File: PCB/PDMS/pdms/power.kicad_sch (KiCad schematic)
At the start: 32 parts, among them IC10 LDO40LPU50RY, IC11 MP2332HGTL-P, IC14 LDO40LPU50RY, IC3 LDO40LPU33RY, Q1 AO3401A, Q11 AO3401A

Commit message: Finished 2024 version + gerbers
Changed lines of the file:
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@@
   (junction (at 94.615 42.545) (diameter 0) (color 0 0 0 0)
+  )
+  (junction (at 154.813 175.768) (diameter 0) (color 0 0 0 0)
   )
   (junction (at 149.225 45.72) (diameter 0) (color 0 0 0 0)
@@
     (stroke (width 0) (type default) (color 0 0 0 0))
   )
+  (wire (pts (xy 154.813 175.768) (xy 152.527 175.768))
+    (stroke (width 0) (type default) (color 0 0 0 0))
+  )
   (wire (pts (xy 215.265 49.53) (xy 215.265 45.72))
     (stroke (width 0) (type default) (color 0 0 0 0))
@@
     (stroke (width 0) (type default) (color 0 0 0 0))
   )
-  (wire (pts (xy 153.543 175.768) (xy 152.527 175.768))
+  (wire (pts (xy 157.353 175.768) (xy 154.813 175.768))
     (stroke (width 0) (type default) (color 0 0 0 0))
   )
@@
     (pin "1")
   )
-  (symbol (lib_id "power:+12VA") (at 153.543 175.768 270) (unit 1)
-    (in_bom yes) (on_board yes) (fields_autoplaced)
-    (property "Reference" "#PWR0136" (id 0) (at 149.733 175.768 0)
-      (effects (font (size 1.27 1.27)) hide)
-    )
-    (property "Value" "+12VA" (id 1) (at 157.226 175.7679 90)
-      (effects (font (size 1.27 1.27)) (justify left))
-    )
-    (property "Footprint" "" (id 2) (at 153.543 175.768 0)
-      (effects (font (size 1.27 1.27)) hide)
-    )
-    (property "Datasheet" "" (id 3) (at 153.543 175.768 0)
+  (symbol (lib_id "power:+12VA") (at 157.353 175.768 270) (unit 1)
+    (in_bom yes) (on_board yes) (fields_autoplaced)
+    (property "Reference" "#PWR0136" (id 0) (at 153.543 175.768 0)
+      (effects (font (size 1.27 1.27)) hide)
+    )
+    (property "Value" "+12VA" (id 1) (at 161.036 175.7679 90)
+      (effects (font (size 1.27 1.27)) (justify left))
+    )
+    (property "Footprint" "" (id 2) (at 157.353 175.768 0)
+      (effects (font (size 1.27 1.27)) hide)
+    )
+    (property "Datasheet" "" (id 3) (at 157.353 175.768 0)
       (effects (font (size 1.27 1.27)) hide)
     )
@@
       (effects (font (size 1.27 1.27)) hide)
     )
+    (pin "1")
+  )
+  (symbol (lib_id "power:PWR_FLAG") (at 154.813 175.768 0) (unit 1)
+    (in_bom yes) (on_board yes)
+    (property "Reference" "#FLG0108" (id 0) (at 154.813 173.863 0)
+      (effects (font (size 1.27 1.27)) hide)
+    )
+    (property "Value" "PWR_FLAG" (id 1) (at 154.686 168.021 90))
+    (property "Footprint" "" (id 2) (at 154.813 175.768 0)
+      (effects (font (size 1.27 1.27)) hide)
+    )
+    (property "Datasheet" "~" (id 3) (at 154.813 175.768 0)
+      (effects (font (size 1.27 1.27)) hide)
+    )

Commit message: Clean-up of schematics
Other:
- note added: "BUCK 3.3V - INTERNAL"
- note added: "POWER SUPPLY SECTION"
- note added: "PROTECTED BATT SUPPLY - EXTERNAL"
- note removed: "BUCK SECTION 3.3V"
- note removed: "POWER SECTION"
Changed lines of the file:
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@@
     (effects (font (size 2 2) italic) (justify left bottom))
   )
-  (text "POWER SECTION" (at 187.325 190.5 0)
-    (effects (font (size 1.8 1.8)) (justify left bottom))
-  )
-  (text "BUCK SECTION 3.3V " (at 116.205 23.495 0)
+  (text "POWER SUPPLY SECTION" (at 186.436 190.754 0)
+    (effects (font (size 1.8 1.8) italic) (justify left bottom))
+  )
+  (text "BUCK 3.3V - INTERNAL" (at 116.205 23.495 0)
     (effects (font (size 2 2)) (justify left bottom))
   )
@@
   (text "X7R capacitors close to pins" (at 153.67 147.32 0)
     (effects (font (size 1 1)) (justify left bottom))
+  )
+  (text "PROTECTED BATT SUPPLY - EXTERNAL" (at 131.699 158.115 0)
+    (effects (font (size 2 2) italic) (justify left bottom))
   )
   (text "REVERSE POLARITY" (at 26.67 93.98 0)
@@
   (symbol (lib_id "pdms_additional:LDO40LPU33RY") (at 51.943 169.418 0) (unit 1)
     (in_bom yes) (on_board yes) (fields_autoplaced)
-    (property "Reference" "IC3" (id 0) (at 67.183 156.21 0))
-    (property "Value" "LDO40LPU33RY" (id 1) (at 67.183 158.75 0))
+    (property "Reference" "IC3" (id 0) (at 67.183 161.29 0))
+    (property "Value" "LDO40LPU33RY" (id 1) (at 67.183 163.83 0))
     (property "Footprint" "PDMS_Additional:SON95P300X300X90-7N-D" (id 2) (at 51.943 169.418 0)
       (effects (font (size 1.27 1.27)) hide)
@@
       (effects (font (size 1.27 1.27)) hide)
     )
-    (property "Reference_1" "IC" (id 4) (at 67.183 161.29 0))
-    (property "Value_1" "LDO40LPU33RY" (id 5) (at 67.183 163.83 0))
+    (property "Reference_1" "IC" (id 4) (at 67.183 163.83 0)
+      (effects (font (size 1.27 1.27)) hide)
+    )
+    (property "Value_1" "LDO40LPU33RY" (id 5) (at 67.183 163.83 0)
+      (effects (font (size 1.27 1.27)) hide)
+    )
     (property "Footprint_1" "SON95P300X300X90-7N-D" (id 6) (at 78.613 264.338 0)
       (effects (font (size 1.27 1.27)) (justify left top) hide)

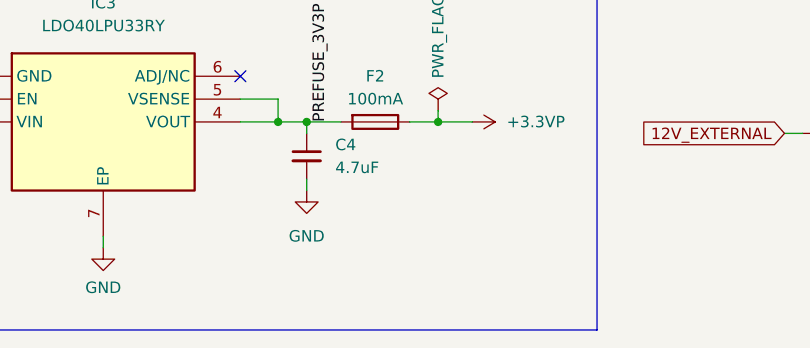
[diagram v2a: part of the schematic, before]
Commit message: Changes after board 4.1 first unit assembly
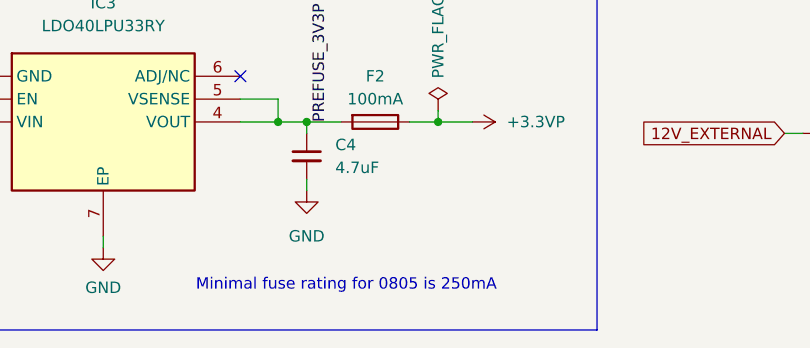
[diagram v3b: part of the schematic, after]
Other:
- note added: "Minimal fuse rating for 0805 is 250mA"
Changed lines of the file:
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@@
     (effects (font (size 2 2) italic) (justify left bottom))
+  )
+  (text "Minimal fuse rating for 0805 is 250mA" (at 77.47 193.421 0)
+    (effects (font (size 1.27 1.27)) (justify left bottom))
   )
   (text "REVERSE POLARITY" (at 26.67 93.98 0)

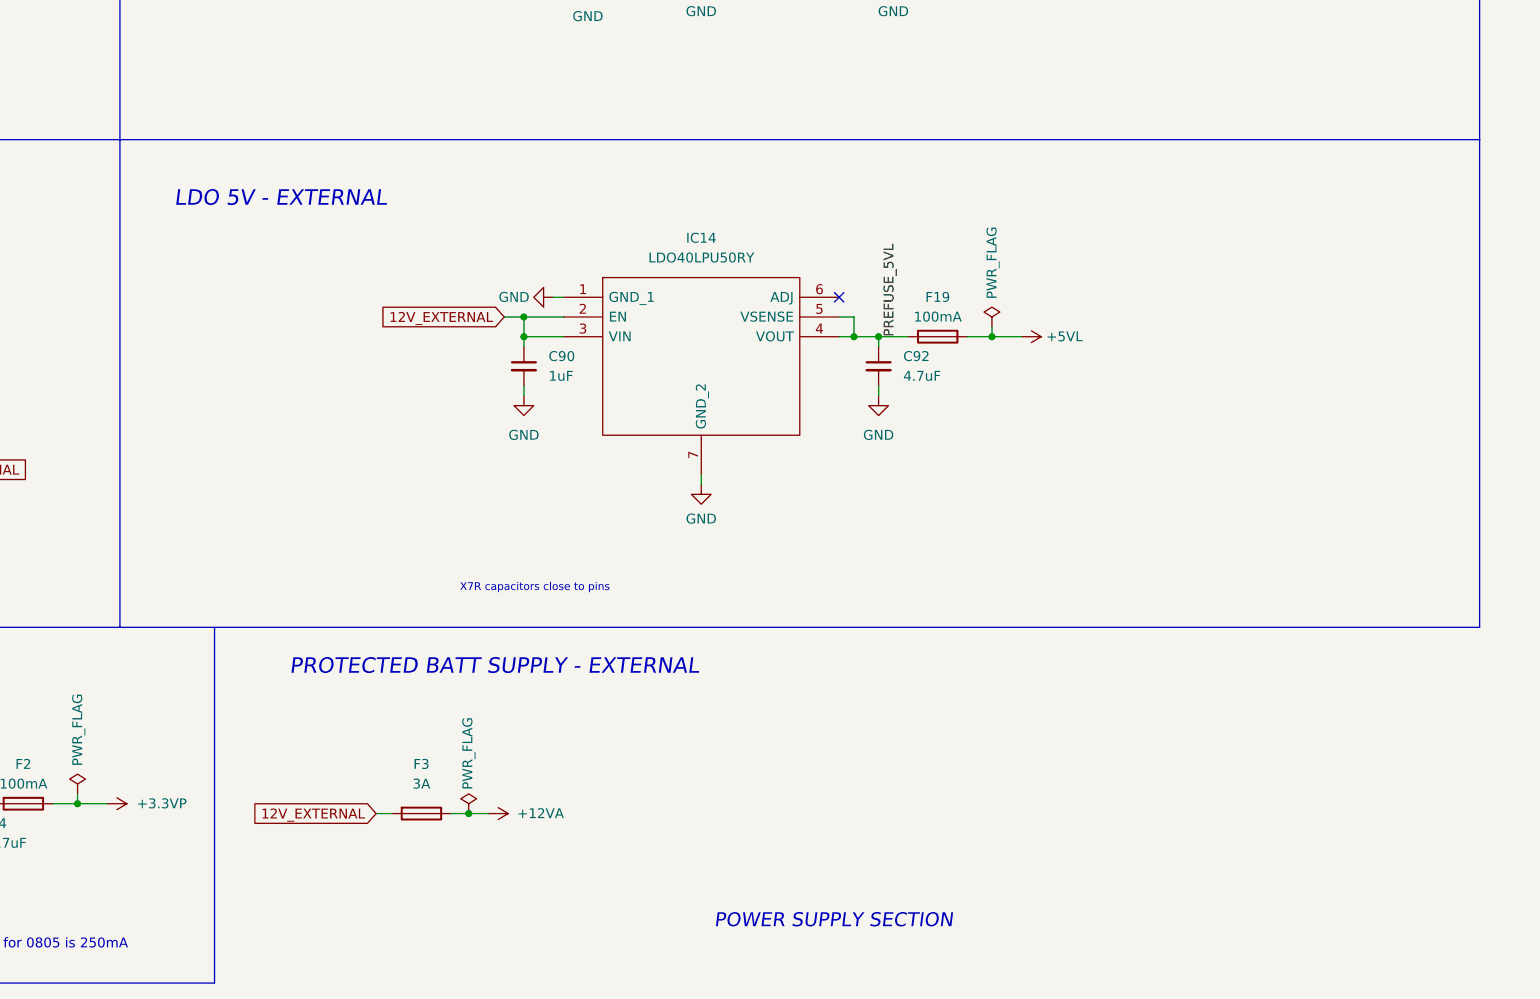
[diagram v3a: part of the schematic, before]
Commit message: Added bigger LDO with lower Rth(ja), TVS suppressor diode
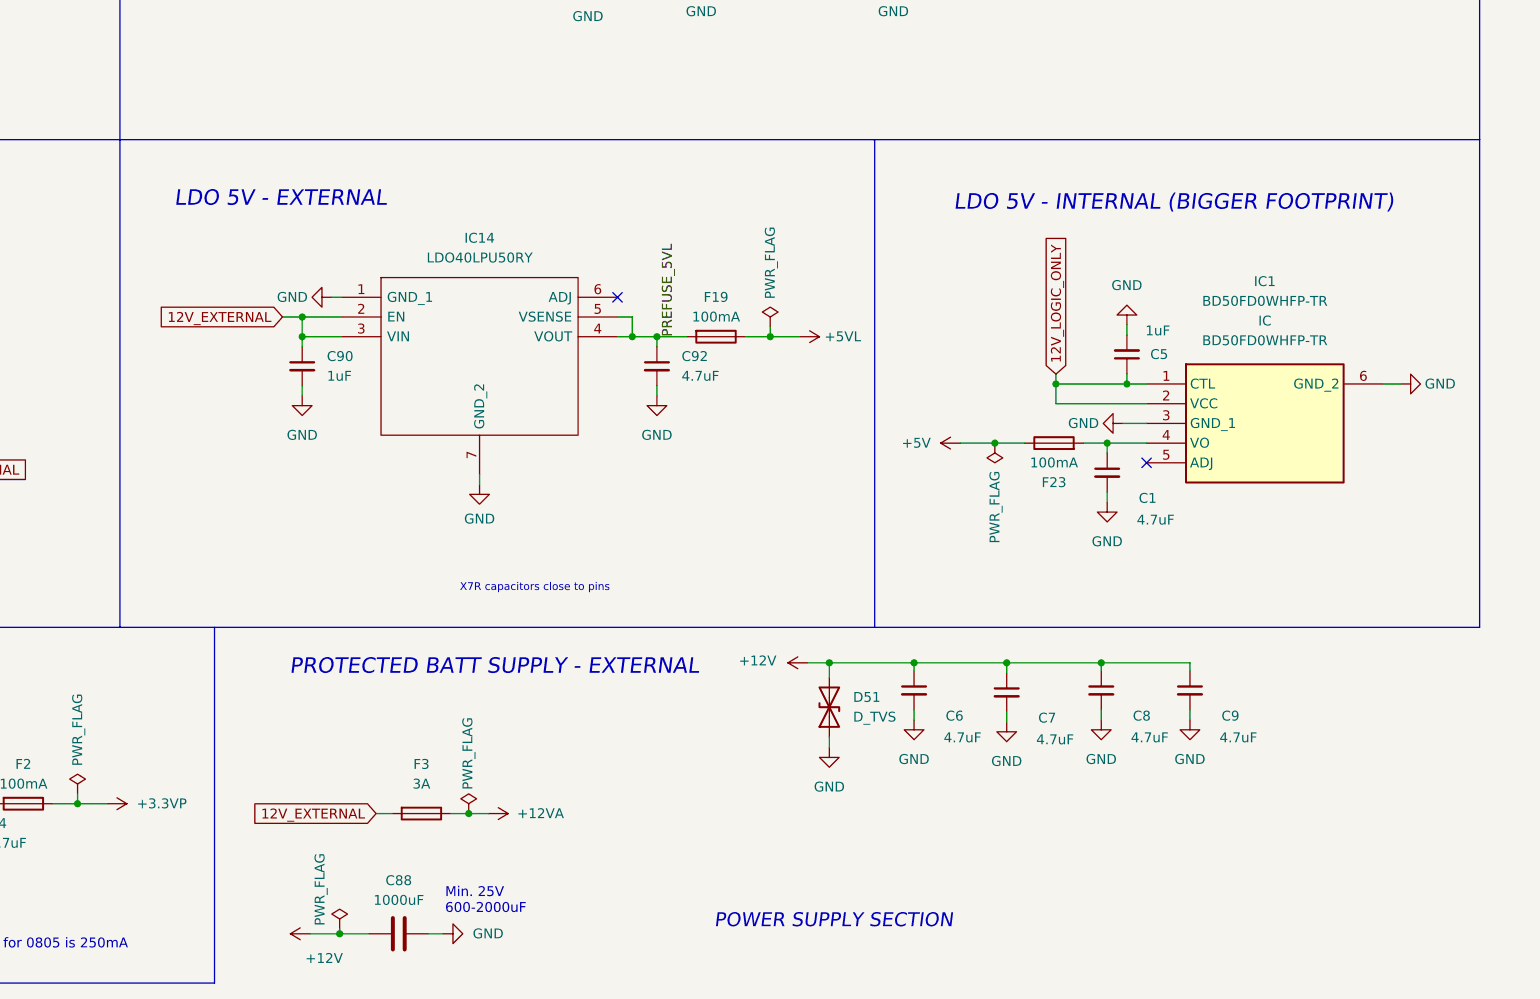
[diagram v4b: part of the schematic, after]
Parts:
- added C1: 4.7uF, Capacitor_SMD:C_0805_2012Metric, symbol Device:C_Small
- added C5: 1uF, Capacitor_SMD:C_0805_2012Metric, symbol Device:C_Small
- added C6, C7, C8, C9: 4.7uF, Capacitor_SMD:C_1206_3216Metric, symbol Device:C_Small
- added C88: 1000uF, Capacitor_THT:CP_Radial_D12.5mm_P5.00mm, symbol Device:C
- added D51: D_TVS, Diode_SMD:D_SMC, symbol Device:D_TVS
- added F23: 100mA, Fuse:Fuse_0805_2012Metric, symbol Device:Fuse
- added IC1: BD50FD0WHFP-TR, PDMS_Additional:BD50FD0WHFPTR, symbol pdms_additional:BD50FD0WHFP-TR
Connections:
- net +12V: now also C6.1, C7.1, C8.1, C88.1, C9.1, D51.2 (A2)
- net +5V: now also F23.1
- net 12V_LOGIC_ONLY: now also C5.1, IC1.1 (CTL), IC1.2 (VCC)
- net GND: now also C1.2, C5.2, C6.2, C7.2, C8.2, C88.2, C9.2, D51.1 (A1), IC1.3 (GND_1), IC1.6 (GND_2)
- new net: C1.1, F23.2, IC1.4 (VO)
- no-connect marks 3 -> 4
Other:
- note added: "LDO 5V - INTERNAL (BIGGER FOOTPRINT)"
- note added: "Min. 25V 600-2000uF"
- moved on the sheet: C90, C92, F19, IC14
